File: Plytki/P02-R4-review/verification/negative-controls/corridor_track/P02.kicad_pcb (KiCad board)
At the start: 2 copper layers, 160 x 100 mm, 139 parts, among them J1 BAT, J14 PWR, J15 VBAT_IN, J2 VMOTOR, Q1 SUP53P06-20, Q2 SUP53P06-20, Q3 2N5551G, Q4 2N5401YBU, Q5 2N5551G, Q6 2N5551G, Q7 2N5551G, Q8 2N5551G, Q9 SUP53P06-20, U1 LM2936Z-5.0, U10 SN74HC08N, U2 LM2903P, U3 TL431BILP, U4 MCP120-450DI/TO, U5 TSR 2-2450, U6 TSR 2-2433, U7 MCP120-300DI/TO, U8 MCP120-450DI/TO, U9 74LVC125A

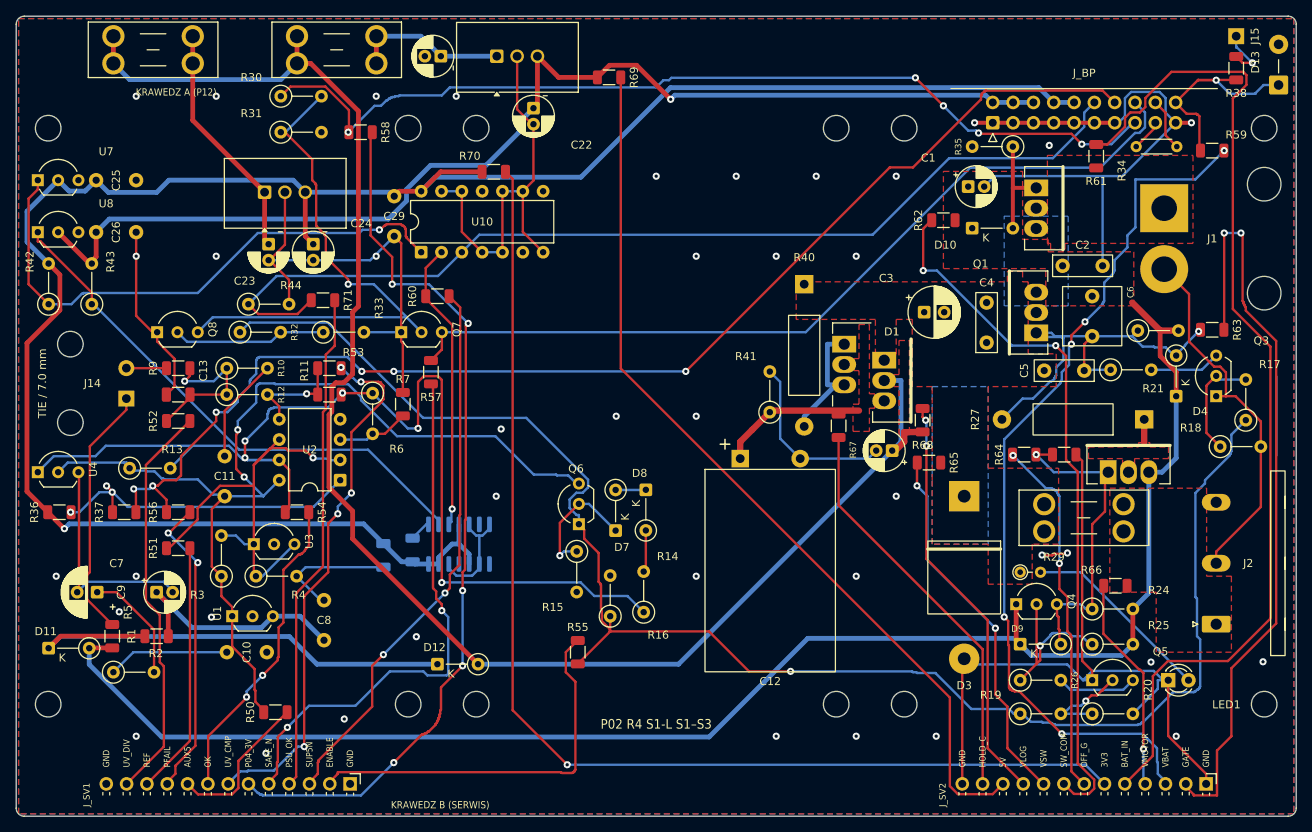
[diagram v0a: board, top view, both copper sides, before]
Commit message: P02 R4 etap 2: rozsunięcie w stronę wolnego pola (wskazanie użytkownika z wydruku 1:1)
Blok sterowania: górna połowa x1,25, dolna x1,12 (układy sztywno z odsprzęganiem i rezystorami
serwisowymi); grupa podtrzymania 8 mm w lewo razem z wylewkami VLOG/HOLD_C i przedłużeniami VSW;
grupa ENABLE 4 mm w lewo; R30, R31, R58, D12 poza strefą H3. Router domknął się w 1. próbie.
DRC bez niepołączeń i innych naruszeń, kontrole PCB 23/23, próby ujemne 12/12, tor 5 A >= 4,1 mm.

Co-Authored-By: Claude Opus 5.5 <noreply@anthropic.com>
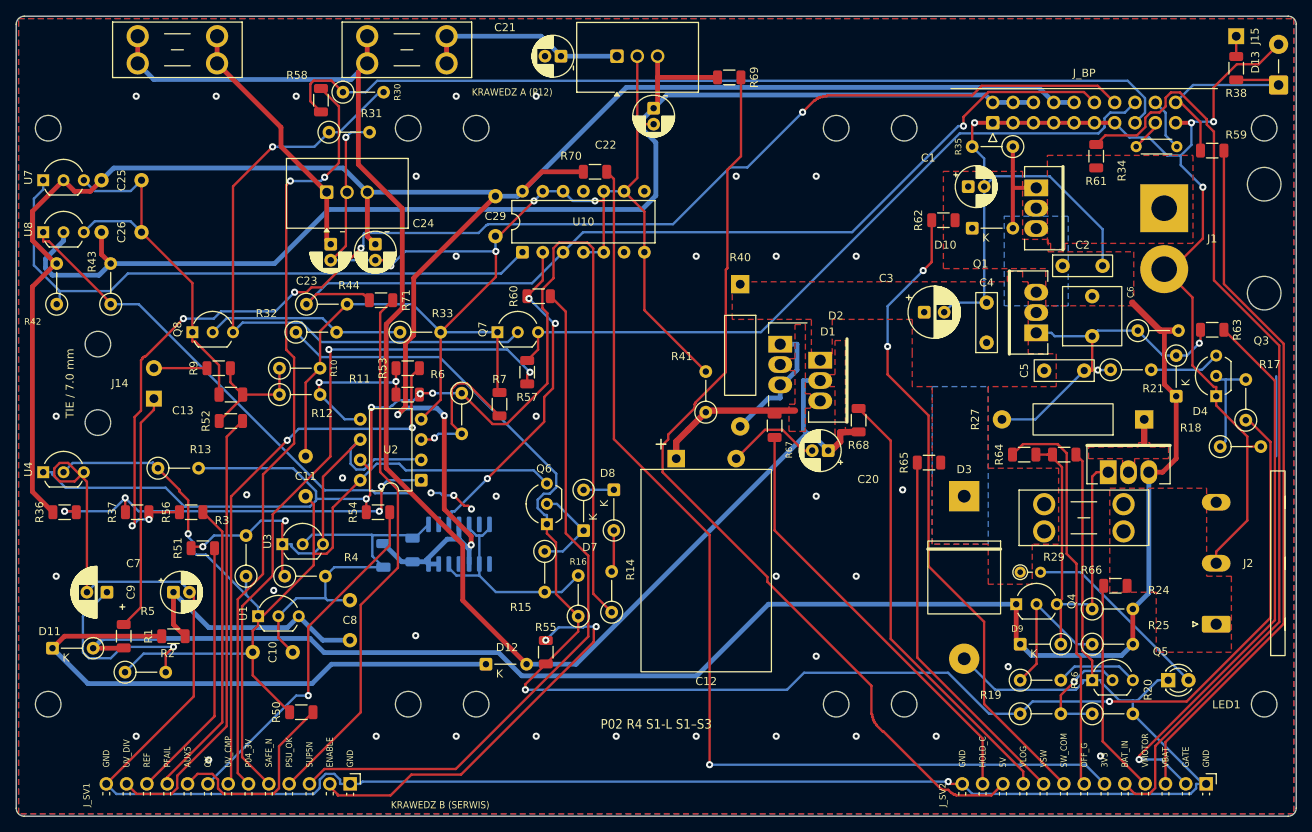
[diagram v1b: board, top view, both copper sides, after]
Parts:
- moved C21 15.0 mm to (68.1, 5.00)
- moved C22 15.0 mm to (79.7, 11.5)
- moved R69 15.0 mm to (89.1, 7.65)
- moved U5 15.0 mm to (75.1, 5.00)
- moved C29 12.7 mm to (59.9, 22.5)
- moved R60 12.7 mm to (65.3, 35.0)
- moved U10 12.7 mm to (63.3, 29.5)
- moved R70 12.7 mm to (72.4, 19.4)
- moved R7 12.1 mm to (60.4, 48.5)
- moved Q7 12.0 mm to (60.2, 39.5)
- moved R57 12.0 mm to (63.9, 44.5)
- moved R6 11.1 mm to (55.7, 47.1)
- moved C11 10.1 mm to (36.2, 60.0)
- moved R54 10.1 mm to (45.2, 62.0)
- moved U2 10.1 mm to (50.6, 58.0)
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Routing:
- net GND: track 448.4 -> 791.4 mm, vias 40 -> 50
- net P02_OK: track 138.3 -> 171.3 mm, vias 5 -> 4
- net /SERW/P02_SV_GATE: track 94.2 -> 70.5 mm, vias 2 -> 1
- net /SERW/P02_SV_VBAT_SENSE: track 109.9 -> 88.4 mm, vias 5 -> 0
- net 5V_SYS: track 145.5 -> 165.6 mm, vias 1 -> 0
- net /SERW/P02_SV_SAFE_N: track 68.6 -> 88.2 mm
- net /SERW/P02_SV_SUP5_N: track 69.4 -> 87.0 mm, vias 2 -> 0
- net /SERW/P02_SV_3V3_IO: track 145.5 -> 129.8 mm
- net SAFE_N: track 106.2 -> 91.3 mm
- net /SERW/P02_SV_P04_3V3: track 111.3 -> 96.7 mm, vias 5 -> 2
- net 3V3_IO: track 261.3 -> 274.1 mm, vias 1 -> 3
- net P02_AUX5: track 140.5 -> 128.1 mm, vias 2 -> 1
- net P02_VLOG: track 200.9 -> 188.7 mm
- net /STER/P02_FAULT_B: track 67.8 -> 79.5 mm
- net /STER/P02_PFAIL_OC: track 41.6 -> 52.5 mm, vias 3 -> 4
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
